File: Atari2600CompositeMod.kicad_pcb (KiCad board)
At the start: 2 copper layers, 42.8 x 21.1 mm, 15 parts, among them J1 AudioIn, J2 input, J3 Composite, Q1 2N3904, Q2 2N3906

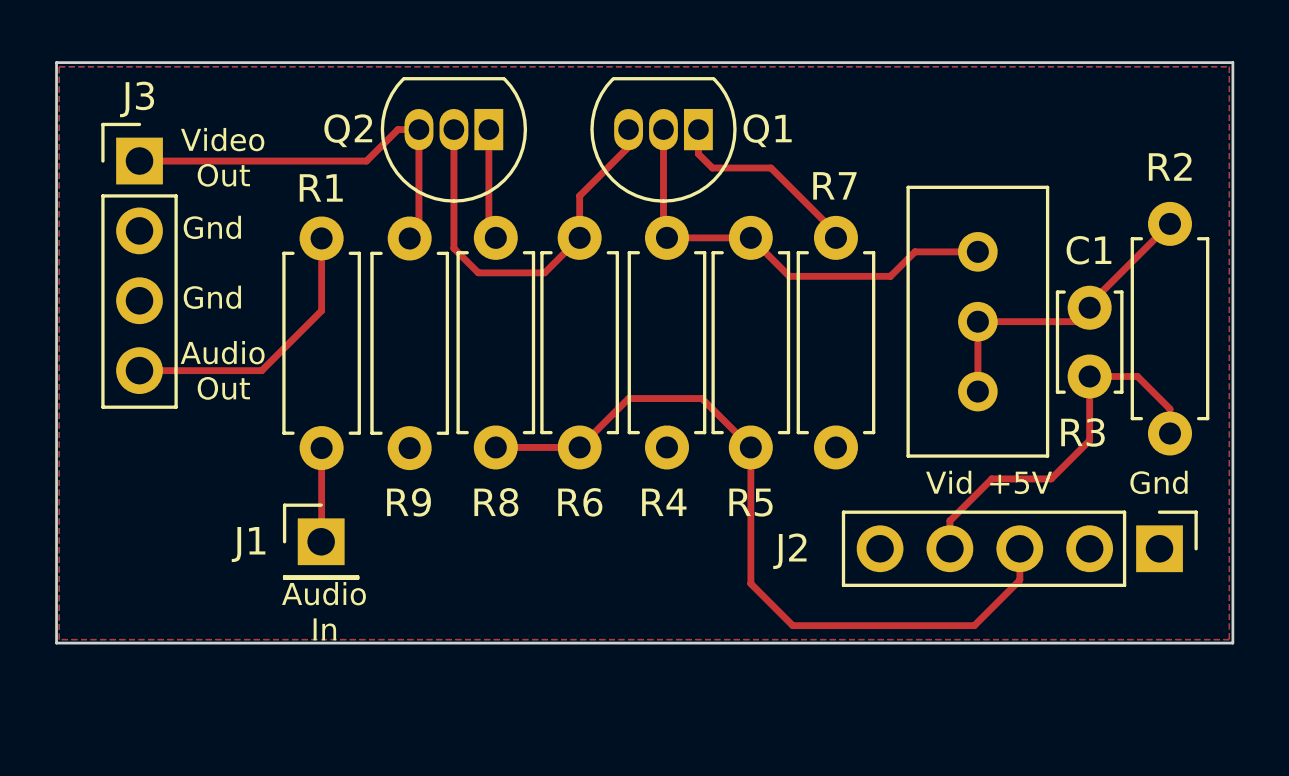
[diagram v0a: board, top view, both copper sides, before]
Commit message: convert board to smd
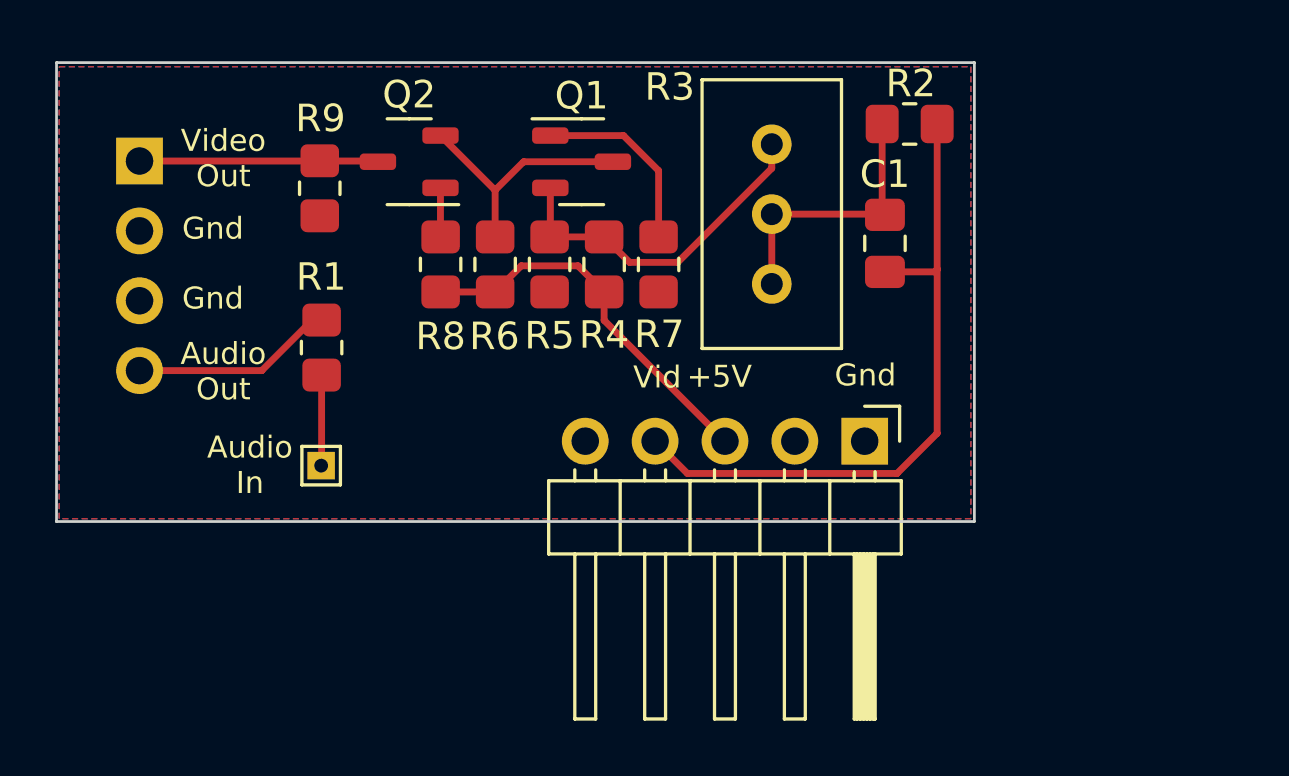
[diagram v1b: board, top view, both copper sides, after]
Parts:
- C1: footprint Capacitor_THT:C_Disc_D3.4mm_W2.1mm_P2.50mm -> Capacitor_SMD:C_0805_2012Metric_Pad1.18x1.45mm_HandSolder
- J1: footprint Connector_PinHeader_2.54mm:PinHeader_1x01_P2.54mm_Vertical -> TestPoint:TestPoint_THTPad_1.0x1.0mm_Drill0.5mm
- J2: footprint Connector_PinHeader_2.54mm:PinHeader_1x05_P2.54mm_Vertical -> Connector_PinHeader_2.54mm:PinHeader_1x05_P2.54mm_Horizontal
- J3: footprint Connector_PinHeader_2.54mm:PinHeader_1x04_P2.54mm_Vertical -> Connector_PinHeader_2.54mm:PinHeader_1x04_P2.54mm_Horizontal; moved to B.Cu
- Q1: value 2N3904 -> MMBT3904; footprint Package_TO_SOT_THT:TO-92_Inline -> Package_TO_SOT_SMD:SOT-23-3
- Q2: value 2N3906 -> MMBT3906; footprint Package_TO_SOT_THT:TO-92_Inline -> Package_TO_SOT_SMD:SOT-23-3
- R1, R2, R4, R5, R6, R7, R8, R9: footprint Resistor_THT:R_Axial_DIN0207_L6.3mm_D2.5mm_P7.62mm_Horizontal -> Resistor_SMD:R_0805_2012Metric_Pad1.20x1.40mm_HandSolder
- moved J2 11.4 mm to (160.0, 108.1)
- moved R2 10.1 mm to (161.6, 96.6), turned to 0 degrees
- moved C1 8.88 mm to (160.7, 100.9)
- moved R4 8.53 mm to (150.5, 101.7)
- moved R3 8.45 mm to (156.6, 97.3)
- moved R8 6.95 mm to (144.6, 101.7)
- moved R7 6.52 mm to (152.5, 101.7)
- moved Q1 4.41 mm to (149.7, 97.9), turned to 0 degrees
- moved R5 4.37 mm to (148.5, 101.7)
- moved R1 3.97 mm to (140.2, 104.7)
- moved R9 3.74 mm to (140.2, 98.9)
- moved R6 3.22 mm to (146.5, 101.7)
- moved Q2 3.12 mm to (143.4, 97.9)
- moved J1 2.77 mm to (140.2, 109.0)
- turned J3 to 180 degrees
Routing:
- net Net-(J2-Pin_3): track 28.1 -> 14.0 mm
- net Net-(J2-Pin_4): track 13.9 -> 24.5 mm
- net VideoOut: track 14.7 -> 8.68 mm
- net Net-(Q1-C): track 14.5 -> 9.22 mm
- net Net-(Q1-B): track 16.2 -> 12.5 mm
- net AudioOut: track 10.2 -> 7.38 mm
- net Net-(Q2-E): track 4.04 -> 1.79 mm
- net Net-(C1-Pad2): track 11.1 -> 10.0 mm
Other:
- board size 42.8 x 21.1 mm -> 33.4 x 16.7 mm
